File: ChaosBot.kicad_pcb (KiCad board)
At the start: 2 copper layers, 68 x 86.6 mm, 69 parts, among them M1 Motor_DC, Q1 NPN, Q2 NPN, SW1 SW_Push

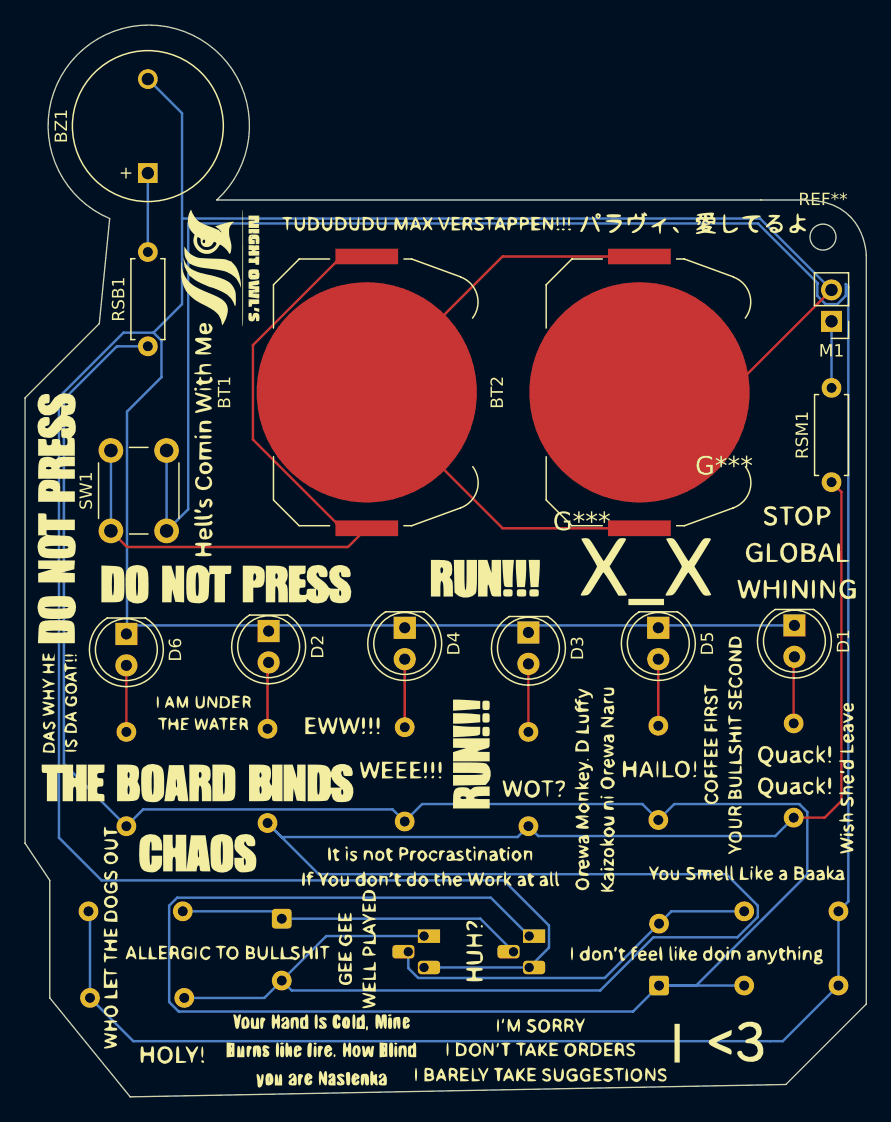
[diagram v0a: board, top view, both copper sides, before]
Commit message: Rotated the battery holder by 90 degree
As it was not possbile to insert the batteries in the previous instance of the PCB
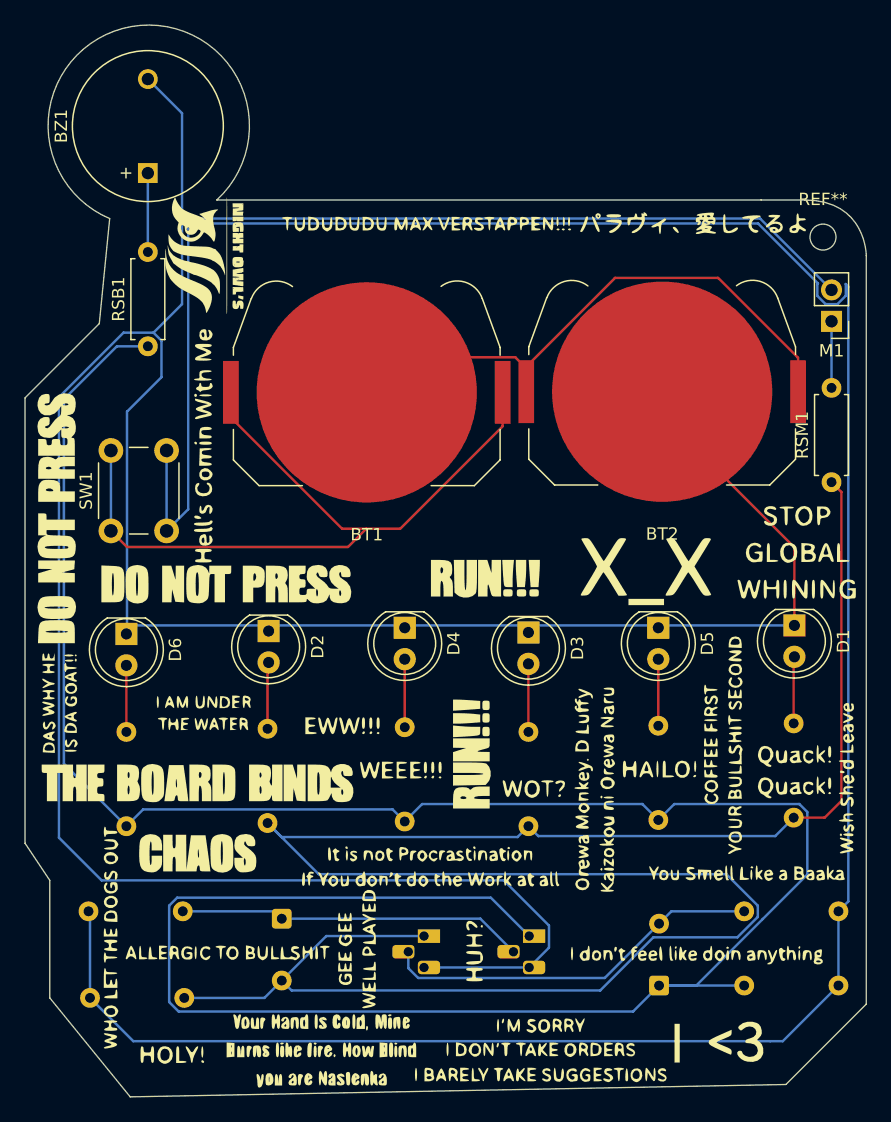
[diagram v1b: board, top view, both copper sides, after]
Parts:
- moved BT2 1.84 mm to (123.5, 76.0), turned to 180 degrees
- moved G*** 1.62 mm to (87.2, 65.0)
- moved G*** 0.50 mm to (86.5, 80.5)
- turned BT1 to 180 degrees
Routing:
- net Net-(BT2--): track 277.0 -> 289.4 mm
- net Net-(BT1--): track 53.2 -> 48.7 mm
- net Net-(BT1-+): track 60.3 -> 62.2 mm

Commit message: Rotated the battery by 180 degree
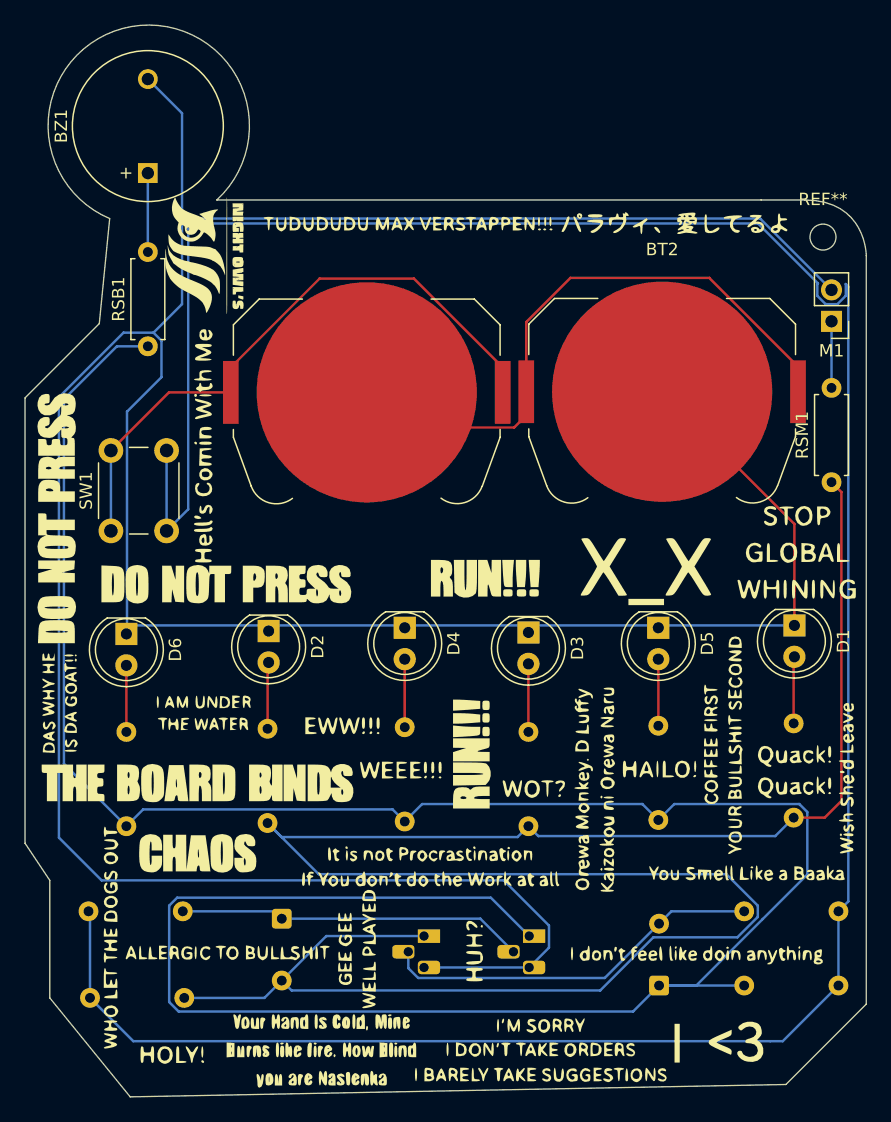
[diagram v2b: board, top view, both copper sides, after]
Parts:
- moved G*** 1.50 mm to (103.0, 62.5)
- moved G*** 1.50 mm to (124.5, 62.5)
- turned BT1 to 0 degrees
- turned BT2 to 0 degrees
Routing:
- net Net-(BT1-+): track 62.2 -> 52.1 mm
- net Net-(BT2--): track 289.4 -> 281.4 mm
- net Net-(BT1--): track 48.7 -> 54.5 mm

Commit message: Added the Links in SS
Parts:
- removed the G*** at (127.0, 68.0)
- removed the G*** at (128.5, 82.0)
- removed the G*** at (91.5, 67.5)
- removed the G*** at (109.5, 72.0)
- removed the G*** at (94.5, 84.0)
- removed the G*** at (129.5, 93.5)
- removed the G*** at (117.0, 86.5)
- added G***: LOGO, LOGO, B.Cu at (97.0, 68.0)
- added G***: LOGO, LOGO, B.Cu at (97.5, 86.5)
- added G***: LOGO, LOGO, B.Cu at (97.0, 74.5)
- added G***: LOGO, LOGO, B.Cu at (97.0, 80.5)
- added G***: LOGO, LOGO, B.Cu at (123.5, 77.5)
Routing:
- net Net-(RLA1-Pad2): track 217.8 -> 220.3 mm
